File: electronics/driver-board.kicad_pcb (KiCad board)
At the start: 2 copper layers, 40 x 40 mm, 49 parts, among them J3 S4B-XH-A, J4 Qwiic_RA, J5 Conn_01x06_Female, J7 Conn_01x02, SW1 SW_Push, SW2 SW_Push, SW3 SW_Push, SW4 SW_Push, U1 LMR16006YQ3, U3 ESP32-C6-MINI-1/U, U5 TMC5240-TSSOP38, U7 AS5047D

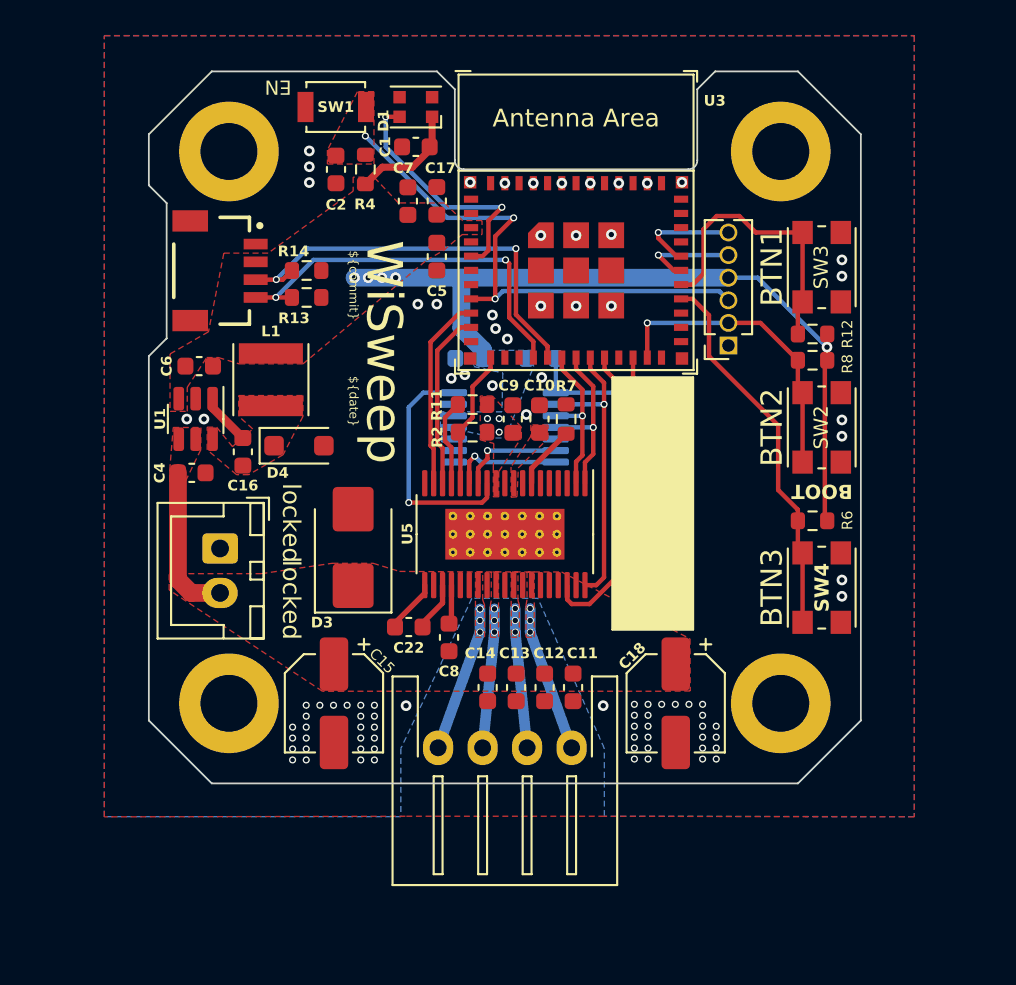
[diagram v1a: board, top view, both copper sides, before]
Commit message: changed rgb led and updated routing/tracks
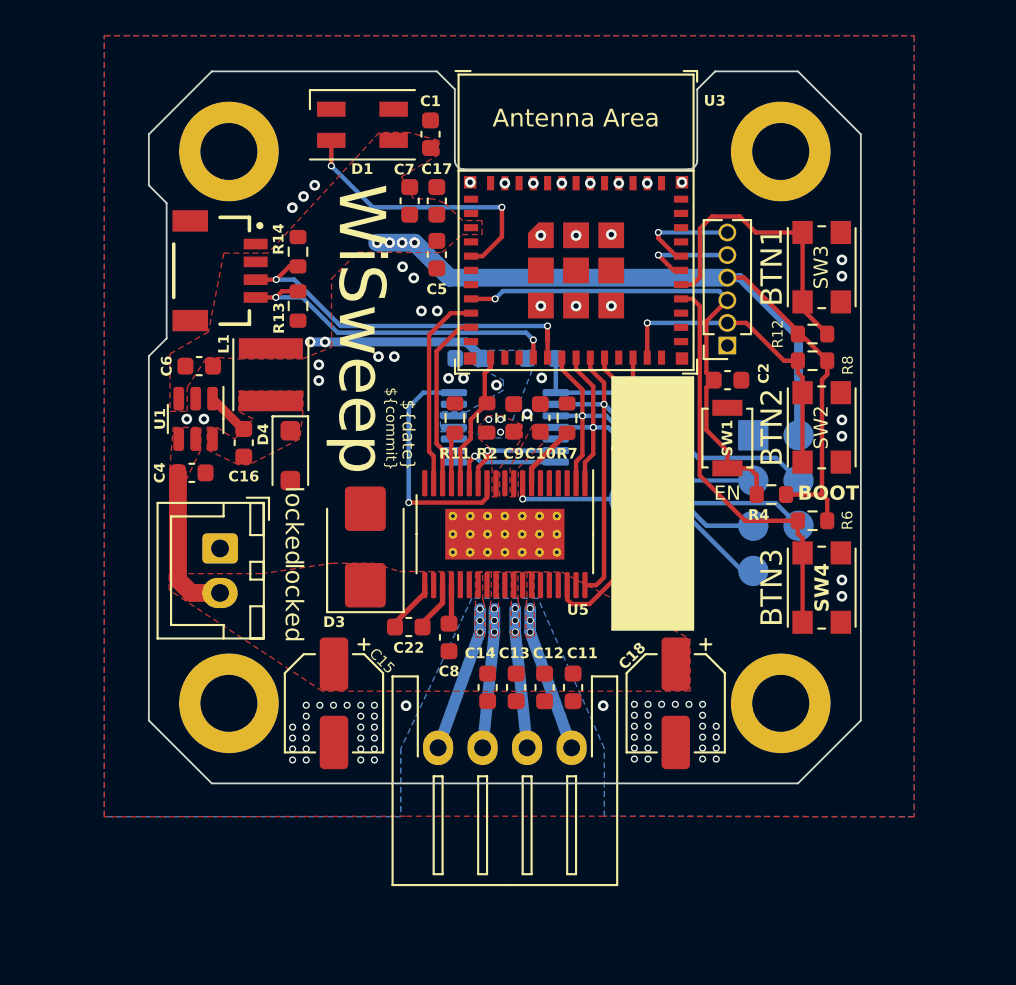
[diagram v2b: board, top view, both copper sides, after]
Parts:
- added J8: Conn_01x08_Socket, Connector_PinHeader_2.54mm:PinHeader_2x04_P2.54mm_Vertical, B.Cu at (66.5, 50.4)
- added J9: Conn_01x01_Socket, TestPoint:TestPoint_Pad_D2.0mm, B.Cu at (56.8, 54.0)
- D1: footprint LED_SMD:LED_WS2812B-2020_PLCC4_2.0x2.0mm -> LED_SMD:LED_SK6812MINI_PLCC4_3.5x3.5mm_P1.75mm
- moved R4 29.2 mm to (65.0, 53.8), turned to 180 degrees
- moved SW1 28.8 mm to (62.5, 50.6), turned to 90 degrees
- moved C2 25.0 mm to (62.5, 47.3), turned to 0 degrees
- moved D1 3.16 mm to (42.0, 33.0)
- moved R11 1.25 mm to (47.2, 49.5), turned to -90 degrees
- moved R14 1.16 mm to (38.4, 40.1), turned to 90 degrees
- moved R2 1.14 mm to (49.0, 49.5), turned to 90 degrees
- moved C1 1.09 mm to (45.8, 33.5), turned to 90 degrees
- moved D4 0.74 mm to (37.9, 51.6), turned to -90 degrees
- moved D3 0.69 mm to (42.2, 56.7)
- moved R13 0.68 mm to (38.4, 43.2), turned to -90 degrees
- moved C16 0.51 mm to (35.3, 50.9)
- moved L1 0.28 mm to (36.9, 47.0)
- moved C5 0.10 mm to (46.2, 40.3)
- moved C7 0.10 mm to (44.7, 37.3)
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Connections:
- R11 pad 1: +3V3 -> GND
- R7 pad 1: Net-(U5-IREF) -> GND
- R7 pad 2: GND -> Net-(U5-IREF)
- U5 pad 8: unconnected-(U5-AIN-Pad8) -> Net-(J9-Pin_1)
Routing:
- net /SPI_SDO: track 9.44 -> 24.1 mm
- net /SPI_CSN_ENC: track 8.23 -> 19.6 mm
- net /SPI_SDI: track 10.2 -> 21.5 mm
- net /SPI_CSN_TMC: track 16.8 -> 27.5 mm, vias 0 -> 1
- net +3V3: track 50.1 -> 60.5 mm, vias 8 -> 9
- net /SPI_SCK: track 16.8 -> 26.9 mm
- net Net-(J9-Pin_1): track 0.00 -> 6.73 mm, vias 0 -> 1
- net /I2C_SCL: track 22.0 -> 19.0 mm
- net /SW_BTN3: track 21.8 -> 23.5 mm
- net /I2C_SDA: track 23.3 -> 21.6 mm
- net Net-(D1-DIN): track 14.6 -> 16.2 mm
- net /ESP_EN: track 30.1 -> 28.5 mm, vias 3 -> 1
- net Net-(U5-UART_EN): track 4.87 -> 3.39 mm
- net GND: vias 87 -> 90
- removed copper zone on F.Cu, net /ESP_EN
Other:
- board text added: "AIN"

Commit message: updates to traces
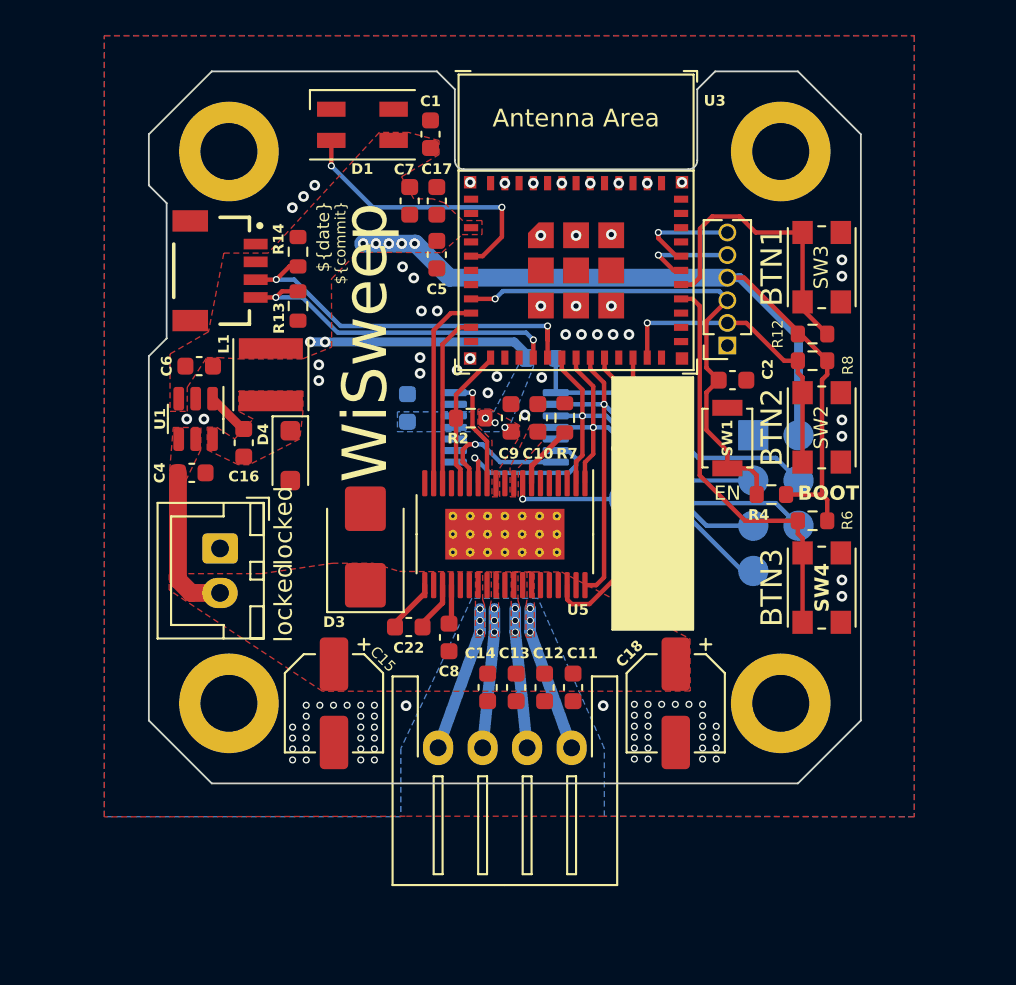
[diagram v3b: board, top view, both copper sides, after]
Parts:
- removed R11: 10k, Resistor_SMD:R_0603_1608Metric
- moved C3 4.44 mm to (44.5, 48.9), turned to -90 degrees
- moved R2 0.91 mm to (48.1, 49.5), turned to 180 degrees
- moved C2 0.28 mm to (62.8, 47.3)
- moved C9 0.15 mm to (50.3, 49.5)
- moved C10 0.14 mm to (51.9, 49.5)
- moved R7 0.13 mm to (53.4, 49.5)
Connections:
- U5 pad 16: Net-(U5-UART_EN) -> unconnected-(U5-UART_EN-Pad16)
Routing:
- net /ENCN: track 13.5 -> 6.48 mm
- net /ENCB: track 5.91 -> 9.44 mm
- net Net-(U5-UART_EN): track 3.39 -> 0.00 mm
- net +3V3: track 60.5 -> 63.8 mm, vias 9 -> 10
- net /ENCA: track 6.38 -> 7.83 mm
- net GND: vias 90 -> 96

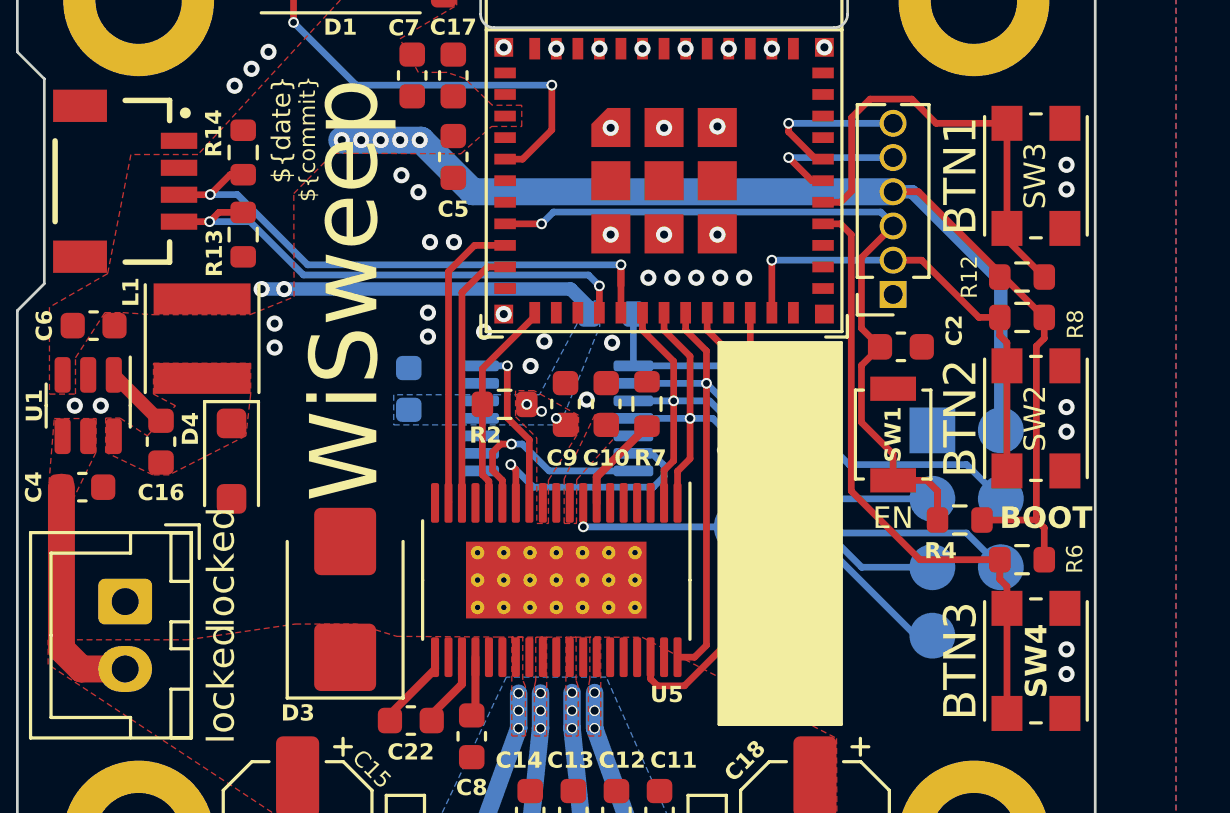
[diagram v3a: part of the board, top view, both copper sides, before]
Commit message: moved more traces around
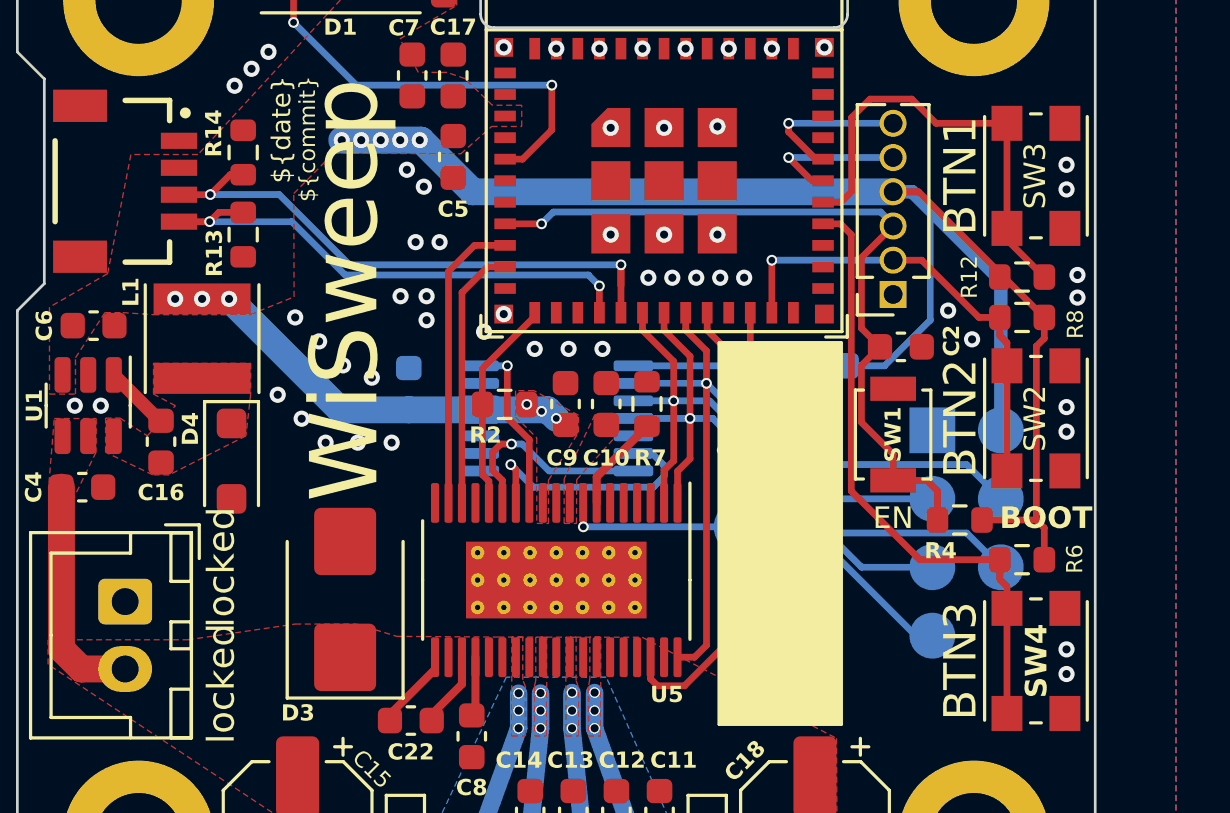
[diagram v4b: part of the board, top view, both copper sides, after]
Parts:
- moved R1 8.19 mm to (60.0, 48.0), turned to 0 degrees
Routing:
- net +3V3: track 63.8 -> 75.9 mm, vias 10 -> 11
- net /SPI_CSN_ENC: track 19.6 -> 20.6 mm
- net GND: vias 96 -> 107
- removed copper zone on B.Cu, net +3V3
